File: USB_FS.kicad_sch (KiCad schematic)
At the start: 0 parts

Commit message: Latest updates
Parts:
- added P1: USB_C_Plug, EasyEDA:USB-SMD_TYPE-C16PCB1.6073, symbol Connector:USB_C_Plug
- added R15, R16: 22, symbol Device:R
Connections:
- new net: P1.A6 (D+), R16.2
- new net: P1.A7 (D-), R15.2
- new net: P1.A4 (VBUS), P1.A9 (VBUS), P1.B4 (VBUS), P1.B9 (VBUS)
- new net Earth: P1.S1 (SHIELD)
- new net GND: P1.A1 (GND), P1.A12 (GND), P1.B1 (GND), P1.B12 (GND)
- new net USB_DM: R15.1
- new net USB_DP: R16.1
- no-connect marks 0 -> 13

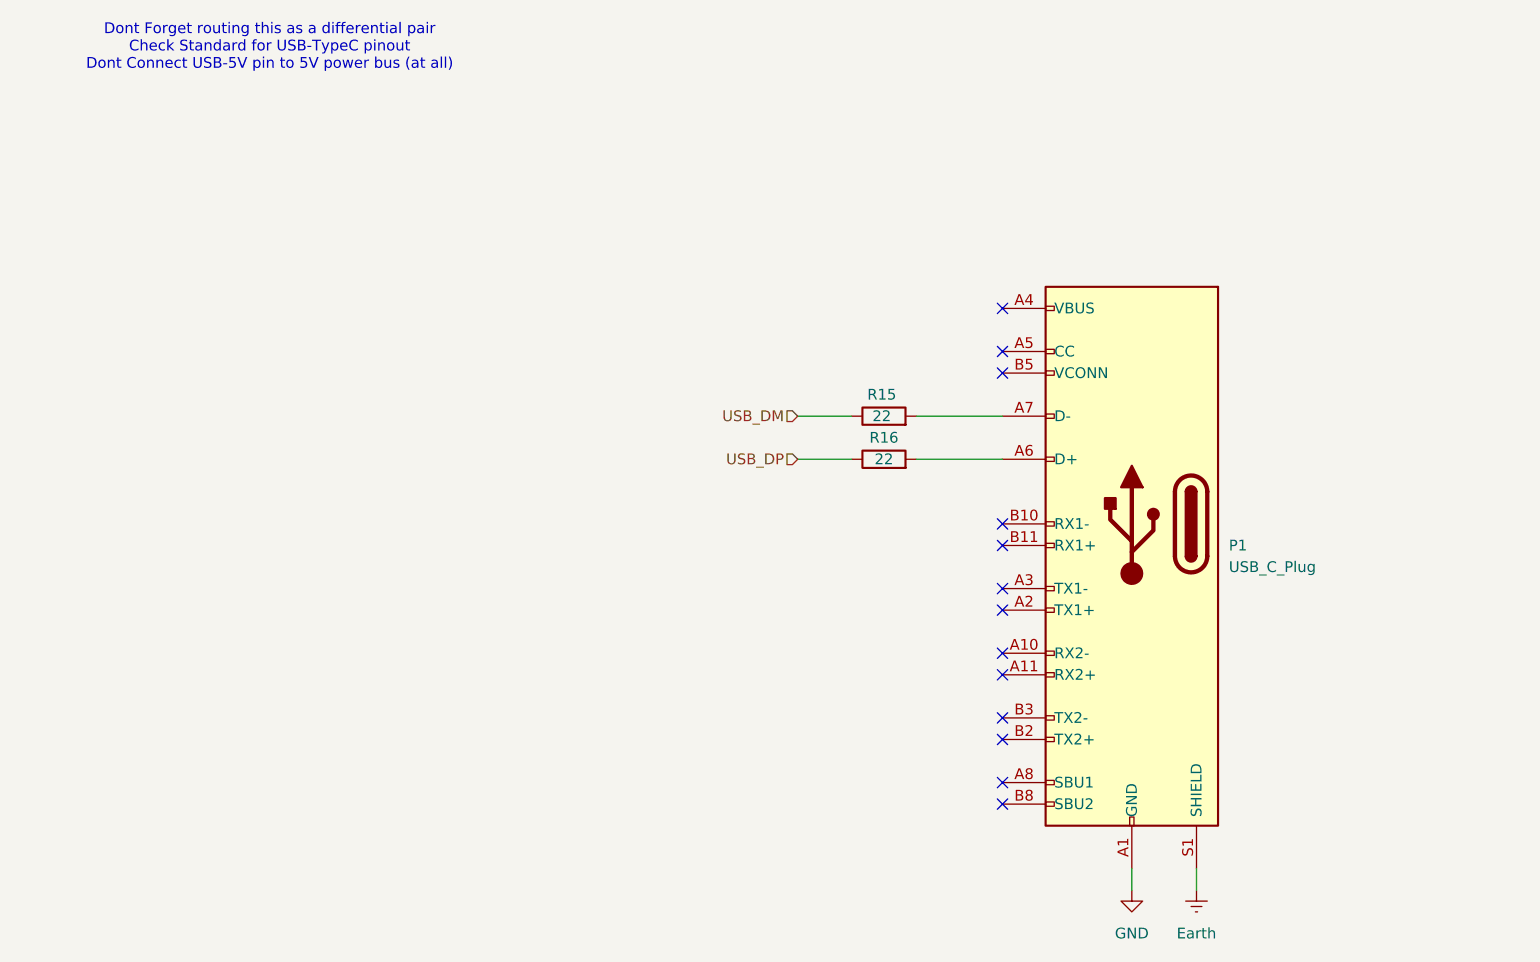
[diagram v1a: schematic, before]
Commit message: Latest changes (added SD , USB , CAN , RS485)
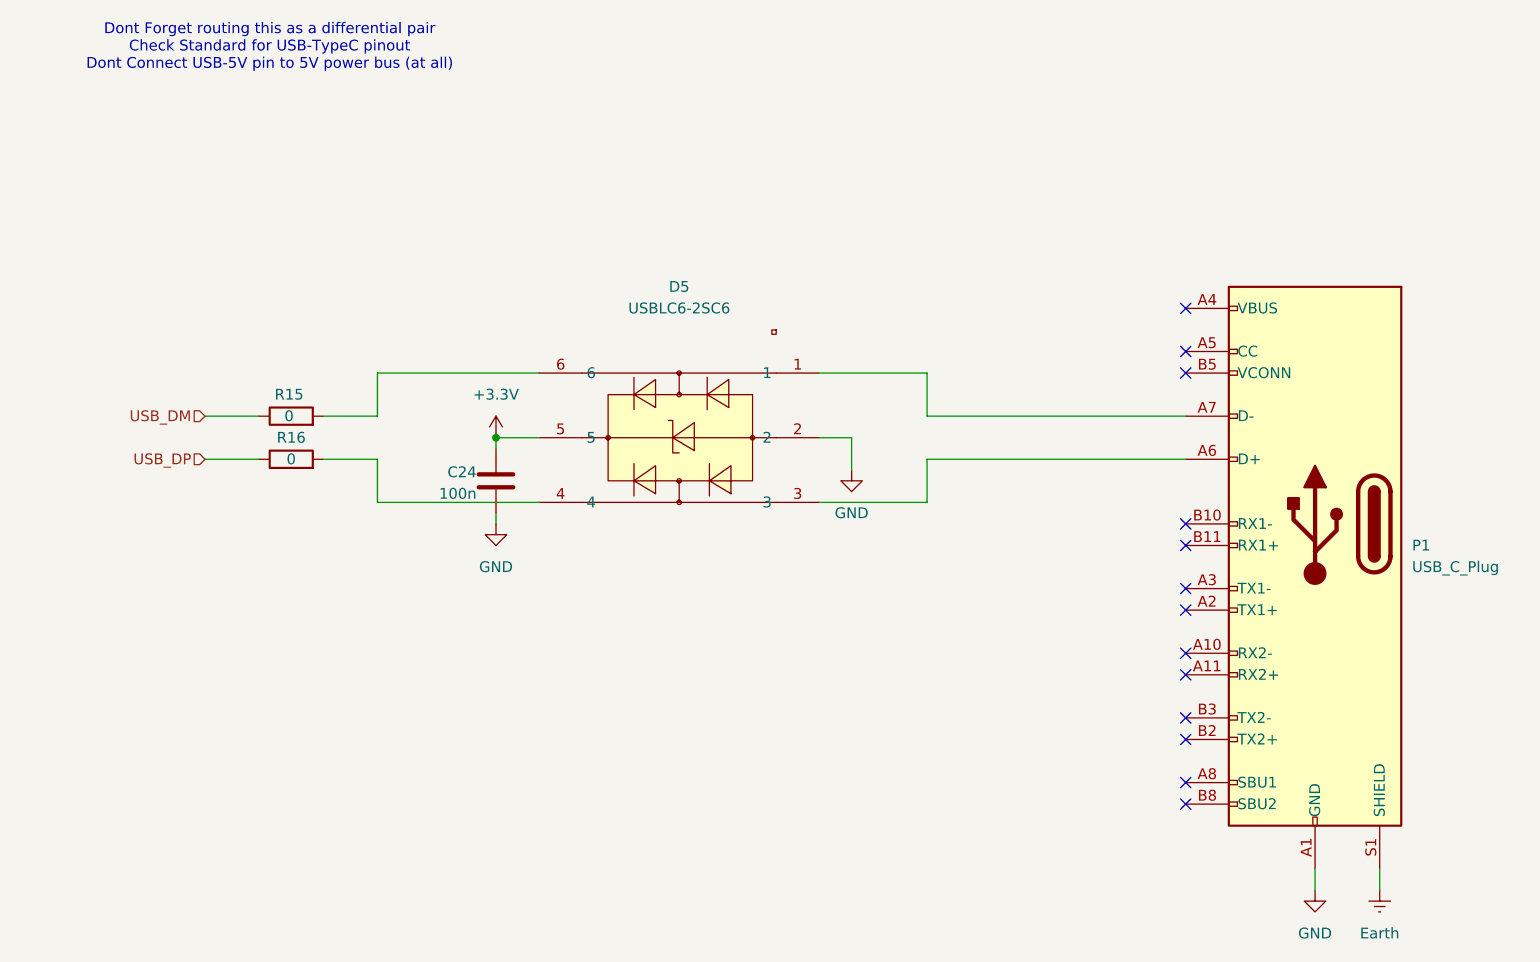
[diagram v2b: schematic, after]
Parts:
- added C24: 100n, symbol Device:C
- added D5: USBLC6-2SC6, EasyEDA:SOT-23-6_L2.9-W1.6-P0.95-LS2.8-BL, symbol EasyEDA:USBLC6-2SC6
- R15, R16: value 22 -> 0
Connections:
- net GND: now also C24.2, D5.2
- net at R16.2: now also D5.4; no longer P1.A6 (D+)
- net at R15.2: now also D5.6; no longer P1.A7 (D-)
- new net: D5.3, P1.A6 (D+)
- new net: D5.1, P1.A7 (D-)
- new net +3.3V: C24.1, D5.5
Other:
- moved on the sheet: P1, R15, R16

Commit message: Schematic--Footprint link
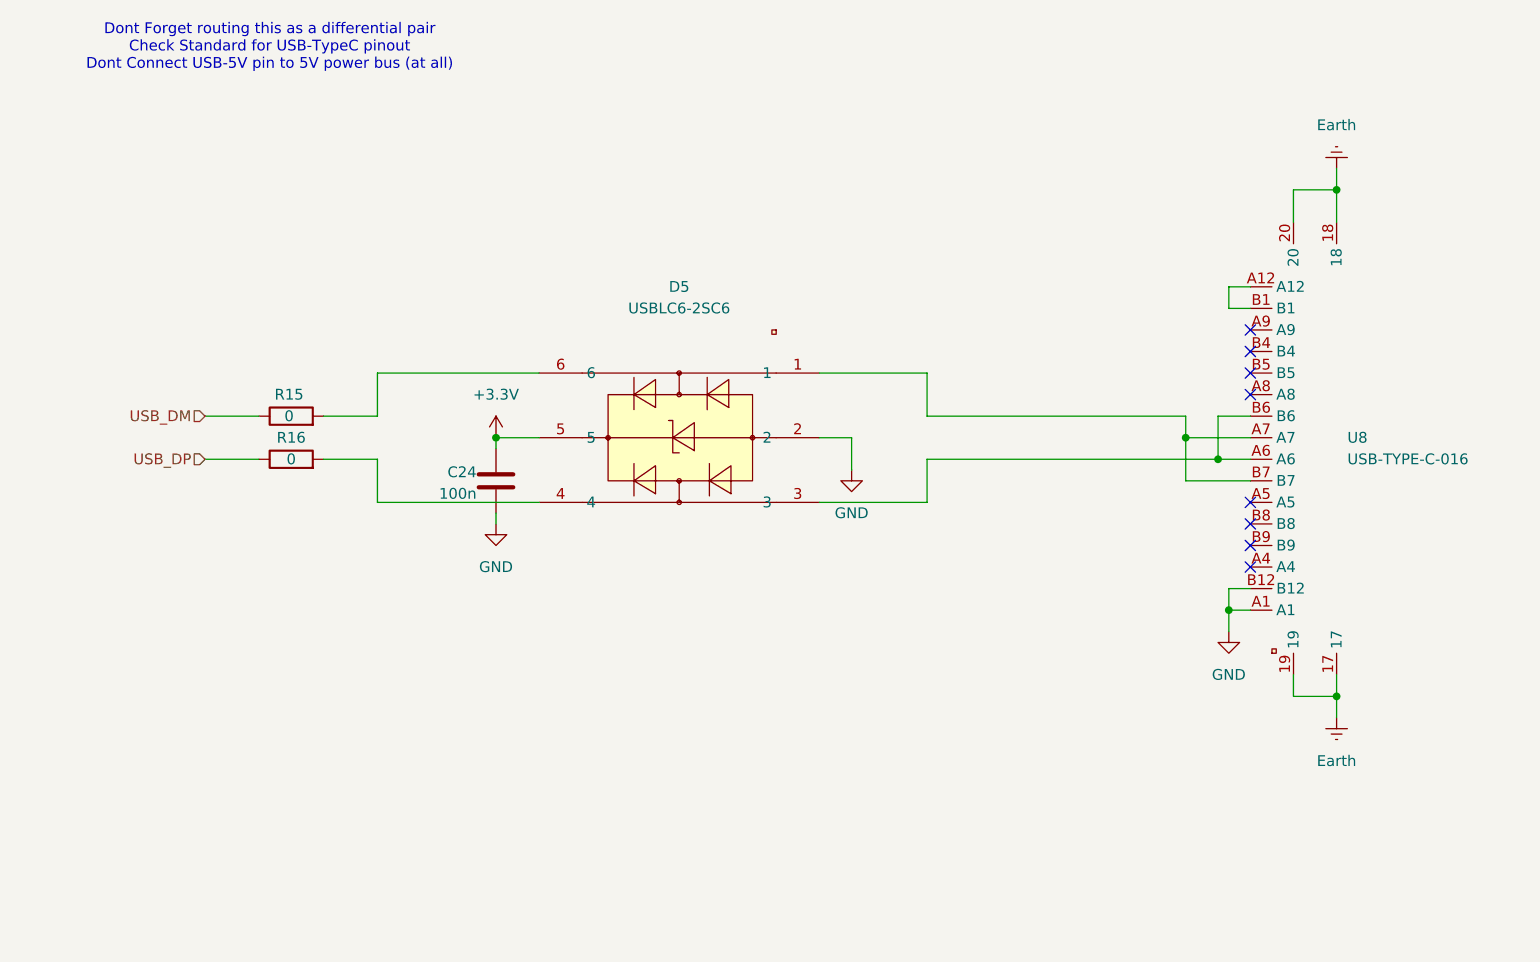
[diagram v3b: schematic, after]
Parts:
- removed P1: USB_C_Plug, EasyEDA:USB-SMD_TYPE-C16PCB1.6073, symbol Connector:USB_C_Plug
- added U8: USB-TYPE-C-016, EasyEDA:USB-SMD_TYPE-C16PCB1.6073, symbol EasyEDA:USB-TYPE-C-016
- C24: footprint (none) -> Capacitor_SMD:C_0805_2012Metric
- R15, R16: footprint (none) -> Resistor_SMD:R_0805_2012Metric
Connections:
- net Earth: now also U8.17, U8.18, U8.19, U8.20
- net GND: now also U8.A1, U8.B12
- net at D5.3: now also U8.A6, U8.B6
- net at D5.1: now also U8.A7, U8.B7
- new net: U8.A12, U8.B1
- no-connect marks 13 -> 8
